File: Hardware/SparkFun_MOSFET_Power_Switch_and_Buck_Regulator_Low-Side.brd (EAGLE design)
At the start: 38.1 x 38.1 mm, 79 parts, among them J1 PTH, J3 5.5x2.1mm Barrel, J4 SMD, Q1 600mA/40V, Q2 100A/100V/6.8mΩ, U1 LMR14203

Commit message: Update silk to match product name
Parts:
- removed U$34: (no value), output:SIDE2
- removed U$35: (no value), output:LOW3
- added U$39: (no value), output:BUCK5
- added U$40: (no value), output:REGULATOR6
- added U$41: (no value), output:#_BUCK_REG7
- added U$42: (no value), output:AND8
- added U$43: (no value), output:LOW0
- added U$44: (no value), output:SIDE0
- moved U$8 29.9 mm to (30.6, 33.7)
- moved U$33 1.01 mm to (35.2, 6.68)
- moved U$23 1.01 mm to (31.4, 6.68)
- moved U$13 0.49 mm to (33.2, 9.38)
- moved U$9 0.49 mm to (33.4, 10.6)
- moved U$2 0.49 mm to (33.4, 11.8)
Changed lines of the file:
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@@
 <layer number="45" name="Holes" color="7" fill="1" visible="yes" active="yes"/>
 <layer number="46" name="Milling" color="3" fill="1" visible="no" active="yes"/>
-<layer number="47" name="Measures" color="7" fill="1" visible="yes" active="yes"/>
+<layer number="47" name="Measures" color="7" fill="1" visible="no" active="yes"/>
 <layer number="48" name="Document" color="7" fill="1" visible="no" active="yes"/>
 <layer number="49" name="Reference" color="7" fill="1" visible="yes" active="yes"/>
@@
 <dimension x1="2.54" y1="0" x2="1.27" y2="8.89" x3="-8.89" y3="4.445" textsize="1.27" layer="47" dtype="vertical" unit="inch"/>
 <text x="8.89" y="53.34" size="1.27" layer="47" font="vector">Units are INCHES</text>
-<wire x1="33.169859375" y1="7.622540625" x2="33.72611875" y2="7.622540625" width="0.2032" layer="21"/>
-<wire x1="19.535140625" y1="11.752575" x2="18.75028125" y2="11.752575" width="0.3048" layer="22"/>
+<wire x1="32.992059375" y1="6.63194375" x2="33.54831875" y2="6.63194375" width="0.2032" layer="21"/>
 <wire x1="25.072340625" y1="22.76348125" x2="25.072340625" y2="20.403821875" width="0.2032" layer="21"/>
 <wire x1="18.313396875" y1="27.523440625" x2="20.67305625" y2="27.523440625" width="0.2032" layer="21"/>
@@
 <dimension x1="0" y1="0" x2="13.78711875" y2="3.5179" x3="6.893559375" y3="-2.745740625" textsize="1.27" layer="47" dtype="horizontal" unit="inch"/>
 <dimension x1="2.54" y1="0" x2="13.78711875" y2="3.520440625" x3="-5.715" y3="1.76021875" textsize="1.27" layer="47" dtype="vertical" unit="inch"/>
+<wire x1="29.842528125" y1="6.175046875" x2="29.84576875" y2="7.1739875" width="0.1524" layer="21" curve="-123.9914"/>
+<wire x1="36.712675" y1="7.13223125" x2="36.709434375" y2="6.133290625" width="0.1524" layer="21" curve="-123.9914"/>
+<wire x1="19.822159375" y1="9.347203125" x2="19.2659" y2="9.347203125" width="0.2032" layer="22"/>
+<wire x1="22.971690625" y1="8.89030625" x2="22.96845" y2="9.889246875" width="0.1524" layer="22" curve="123.9914"/>
+<wire x1="16.10154375" y1="9.847490625" x2="16.104784375" y2="8.84855" width="0.1524" layer="22" curve="123.9914"/>
 </plain>
 <attributes>
@@
 <element name="U$20" library="output" package="#0" value="" x="1.27" y="13.462" smashed="yes" rot="MR270"/>
 <element name="U$22" library="output" package="#1" value="" x="1.27" y="6.35" smashed="yes" rot="MR270"/>
-<element name="U$2" library="output" package="MOSFET0" value="" x="33.54578125" y="11.3512625" smashed="yes"/>
-<element name="U$9" library="output" package="POWER1" value="" x="33.54831875" y="10.119359375" smashed="yes"/>
-<element name="U$13" library="output" package="SWITCH2" value="" x="33.347659375" y="8.930640625" smashed="yes"/>
+<element name="U$2" library="output" package="MOSFET0" value="" x="33.352740625" y="11.803384375" smashed="yes"/>
+<element name="U$9" library="output" package="POWER1" value="" x="33.355278125" y="10.57148125" smashed="yes"/>
+<element name="U$13" library="output" package="SWITCH2" value="" x="33.15461875" y="9.3827625" smashed="yes"/>
 <element name="MEAS" library="SparkFun-Jumpers" package="COMBO-JUMPER_2_NC_TRACE" value="JUMPER-COMBO_2_NC_TRACE" x="5.715" y="16.51" smashed="yes" rot="MR180">
 <attribute name="NAME" x="5.715" y="15.367" size="0.6096" layer="26" font="vector" ratio="20" rot="MR180" align="bottom-center"/>
@@
 <element name="U$7" library="output" package="#ON#10" value="" x="13.843" y="2.2098" smashed="yes"/>
 <element name="LOGO2" library="SparkFun-Aesthetics" package="SFE_LOGO_NAME_FLAME_.2" value="SFE_LOGO_NAME_FLAME.2_INCH" x="18.823940625" y="21.887178125" smashed="yes" rot="MR0"/>
-<element name="U$8" library="SparkFun-Aesthetics" package="SFE_LOGO_FLAME_.2" value="" x="31.2191375" y="3.810003125" smashed="yes"/>
+<element name="U$8" library="SparkFun-Aesthetics" package="SFE_LOGO_FLAME_.2" value="" x="30.5841375" y="33.655003125" smashed="yes"/>
 <element name="PWR_LED" library="SparkFun-Jumpers" package="SMT-JUMPER_2_NC_TRACE_SILK" package3d_urn="urn:adsk.eagle:package:39281/1" value="" x="36.195" y="30.48" smashed="yes" rot="MR90">
 <attribute name="NAME" x="37.338" y="30.48" size="0.6096" layer="26" font="vector" ratio="20" rot="MR90" align="bottom-center"/>
@@
 <element name="FD4" library="SparkFun-Aesthetics" package="FIDUCIAL-MICRO" value="FIDUCIALUFIDUCIAL" x="33.02" y="36.83" smashed="yes"/>
 <element name="U$17" library="output" package="#MEAS#14" value="" x="5.737859375" y="18.209259375" smashed="yes" rot="MR0"/>
-<element name="U$23" library="output" package="LOW0" value="" x="31.607759375" y="7.665721875" smashed="yes"/>
-<element name="U$33" library="output" package="SIDE0" value="" x="35.417759375" y="7.665721875" smashed="yes"/>
-<element name="U$34" library="output" package="SIDE2" value="" x="15.651478125" y="11.79575625" smashed="yes" rot="MR0"/>
-<element name="U$35" library="output" package="LOW3" value="" x="22.136103125" y="11.927834375" smashed="yes" rot="MR0"/>
+<element name="U$23" library="output" package="LOW0" value="" x="31.429959375" y="6.675125" smashed="yes"/>
+<element name="U$33" library="output" package="SIDE0" value="" x="35.239959375" y="6.675125" smashed="yes"/>
 <element name="J6" library="SparkFun-Connectors" package="1X02_NO_SILK" value="" x="8.89" y="36.83" smashed="yes">
 <attribute name="NAME" x="7.62" y="38.227" size="0.6096" layer="25" font="vector" ratio="20"/>
@@
 <element name="U$38" library="output" package="#MEAS#14" value="" x="10.284459375" y="16.532859375" smashed="yes"/>
 <element name="LOGO3" library="SparkFun-Aesthetics" package="ORDERING_INSTRUCTIONS" value="SPECIAL_INSTRUCTIONS-ORDERING" x="64.77" y="50.8" smashed="yes"/>
+<element name="U$39" library="output" package="BUCK5" value="" x="22.96921875" y="10.970259375" smashed="yes" rot="MR0"/>
+<element name="U$40" library="output" package="REGULATOR6" value="" x="17.25421875" y="10.970259375" smashed="yes" rot="MR0"/>
+<element name="U$41" library="output" package="#_BUCK_REG7" value="" x="33.461959375" y="8.072121875" smashed="yes"/>
+<element name="U$42" library="output" package="AND8" value="" x="19.072859375" y="12.430759375" smashed="yes" rot="MR0"/>
+<element name="U$43" library="output" package="LOW0" value="" x="21.384259375" y="9.390384375" smashed="yes" rot="MR0"/>
+<element name="U$44" library="output" package="SIDE0" value="" x="17.574259375" y="9.390384375" smashed="yes" rot="MR0"/>
 </elements>
 <signals>
@@
 <via x="5.466078125" y="10.195559375" extent="1-16" drill="0.3048"/>
 <via x="15.9385" y="4.831078125" extent="1-16" drill="0.3048"/>
-<via x="31.793178125" y="1.3843" extent="1-16" drill="0.3048"/>
-<via x="37.152578125" y="6.215378125" extent="1-16" drill="0.3048"/>
+<via x="32.46881875" y="0.7874" extent="1-16" drill="0.3048"/>
+<via x="37.371015625" y="5.435596875" extent="1-16" drill="0.3048"/>
 <via x="37.203378125" y="32.369759375" extent="1-16" drill="0.3048"/>
 <via x="31.666178125" y="36.91381875" extent="1-16" drill="0.3048"/>

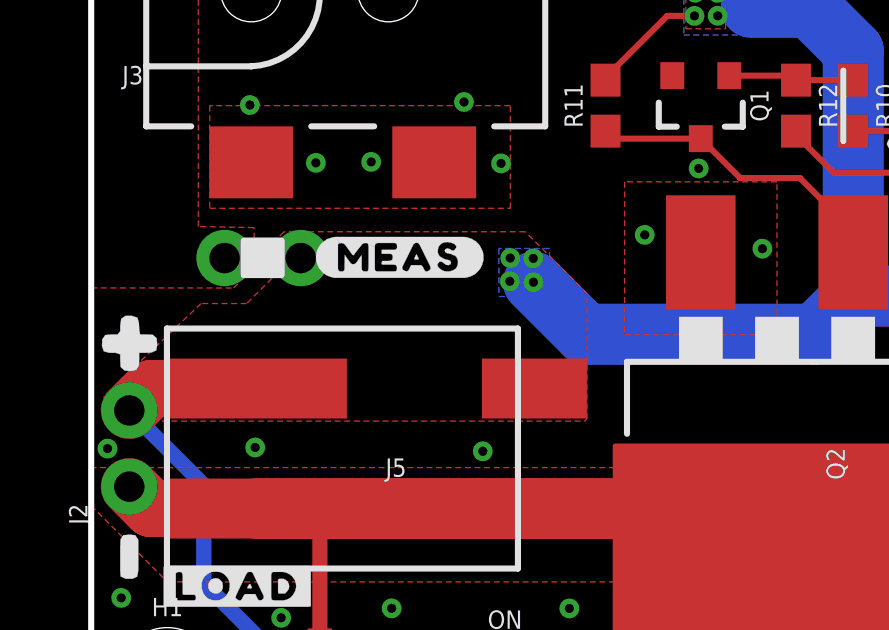
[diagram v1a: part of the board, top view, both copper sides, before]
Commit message: Added D1 Zener
-Added D1 to clamp spike on VCC and protect U1 and C4
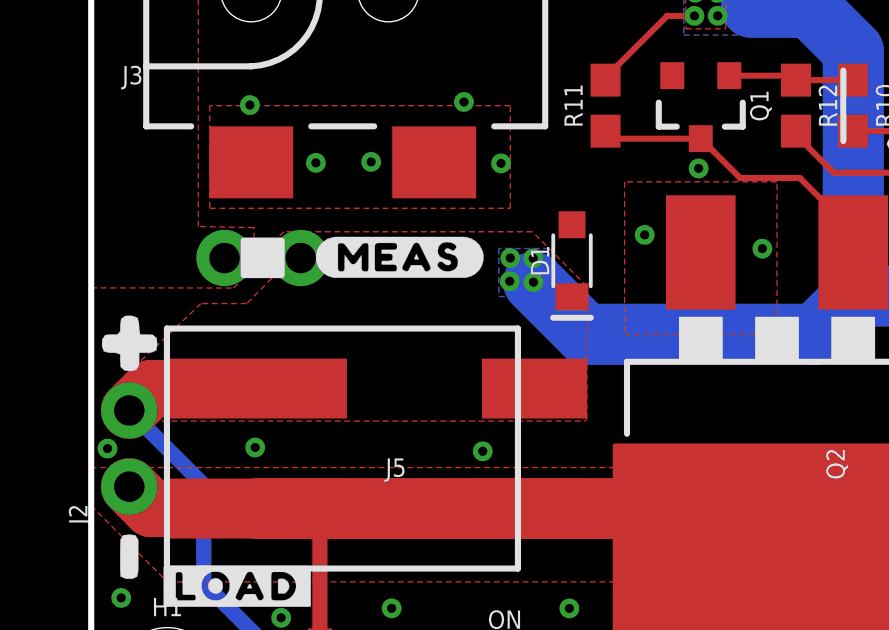
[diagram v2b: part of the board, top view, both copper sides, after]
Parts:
- added D1: 15V, SparkFun-DiscreteSemi:PANASONIC_SMINI2-F5-B
- J4: value SMD -> 1X04_SMD_STRAIGHT_COMBO
- ON, POWER: value RED -> Red
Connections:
- net GND: now also D1.A
- net VCC: now also D1.C
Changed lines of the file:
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@@
 <layer number="27" name="tValues" color="7" fill="1" visible="no" active="yes"/>
 <layer number="28" name="bValues" color="7" fill="1" visible="no" active="yes"/>
-<layer number="29" name="tStop" color="7" fill="6" visible="no" active="yes"/>
+<layer number="29" name="tStop" color="7" fill="6" visible="yes" active="yes"/>
 <layer number="30" name="bStop" color="7" fill="3" visible="no" active="yes"/>
 <layer number="31" name="tCream" color="7" fill="5" visible="no" active="yes"/>
@@
 <attribute name="VALUE" x="2.54" y="33.528" size="0.6096" layer="27" font="vector" ratio="20" align="top-center"/>
 </element>
-<element name="ON" library="SparkFun-LED" package="LED-0603" value="RED" x="13.7922" y="3.5179" smashed="yes">
+<element name="ON" library="SparkFun-LED" package="LED-0603" value="Red" x="13.7922" y="3.5179" smashed="yes">
 <attribute name="NAME" x="13.7922" y="4.1529" size="0.6096" layer="25" font="vector" ratio="20" align="bottom-center"/>
 <attribute name="PROD_ID" value="DIO-17976" x="13.7922" y="7.3279" size="1.778" layer="27" font="vector" ratio="15" display="off"/>
+<attribute name="VALUE" value="Red" x="13.7922" y="3.5179" size="1.778" layer="27" display="off"/>
 </element>
 <element name="R2" library="SparkFun-Resistors" package="0603" value="4.7k" x="10.1498375" y="2.519678125" smashed="yes" rot="R270">
@@
 <attribute name="VALUE" x="5.715" y="17.653" size="0.6096" layer="28" font="vector" ratio="20" rot="MR180" align="top-center"/>
 </element>
-<element name="POWER" library="SparkFun-LED" package="LED-0603" value="RED" x="33.655" y="29.21" smashed="yes">
+<element name="POWER" library="SparkFun-LED" package="LED-0603" value="Red" x="33.655" y="29.21" smashed="yes">
 <attribute name="NAME" x="33.655" y="29.845" size="0.6096" layer="25" font="vector" ratio="20" align="bottom-center"/>
 <attribute name="PROD_ID" value="DIO-17976" x="33.655" y="29.21" size="1.778" layer="27" font="vector" ratio="15" display="off"/>
+<attribute name="VALUE" value="Red" x="33.655" y="29.21" size="1.778" layer="27" display="off"/>
 </element>
 <element name="R1" library="SparkFun-Resistors" package="0603" value="4.7k" x="33.6423" y="30.8737" smashed="yes" rot="R180">
@@
 <element name="U$25" library="output" package="POWER_1" value="" x="18.696940625" y="16.5735" smashed="yes" rot="MR0"/>
 <element name="U$26" library="output" package="SWITCH_2" value="" x="18.760440625" y="14.23161875" smashed="yes" rot="MR0"/>
-<element name="J4" library="SparkFun-Connectors" package="1X04_SMD_VERTICAL_COMBO" value="SMD" x="33.02" y="22.86" smashed="yes" rot="R270">
+<element name="J4" library="SparkFun-Connectors" package="1X04_SMD_VERTICAL_COMBO" value="1X04_SMD_STRAIGHT_COMBO" x="33.02" y="22.86" smashed="yes" rot="R270">
 <attribute name="NAME" x="35.878" y="23.241" size="0.6096" layer="25" font="vector" ratio="20" rot="R270"/>
 <attribute name="PROD_ID" value="CONN-08511" x="33.02" y="22.86" size="1.778" layer="27" rot="R270" display="off"/>
@@
 <element name="U$43" library="output" package="LOW0" value="" x="21.384259375" y="9.390384375" smashed="yes" rot="MR0"/>
 <element name="U$44" library="output" package="SIDE0" value="" x="17.574259375" y="9.390384375" smashed="yes" rot="MR0"/>
+<element name="D1" library="SparkFun-DiscreteSemi" package="PANASONIC_SMINI2-F5-B" value="15V" x="16.0274" y="16.418559375" smashed="yes" rot="R90">
+<attribute name="NAME" x="15.2654" y="16.418559375" size="0.6096" layer="25" font="vector" ratio="20" rot="R90" align="bottom-center"/>
+<attribute name="PROD_ID" value="DIO-12989" x="16.0274" y="16.418559375" size="1.778" layer="27" rot="R90" display="off"/>
+<attribute name="VALUE" x="16.7894" y="16.418559375" size="0.6096" layer="27" font="vector" ratio="20" rot="R90" align="top-center"/>
+</element>
 </elements>
 <signals>
@@
 </polygon>
 <via x="0.543559375" y="10.15745625" extent="1-16" drill="0.3048"/>
+<contactref element="D1" pad="A"/>
 </signal>
 <signal name="SDA1">
@@
 <wire x1="3.75158125" y1="8.94841875" x2="3.75158125" y2="5.6794375" width="0.508" layer="16"/>
 <polygon width="0.2032" layer="1" thermals="no">
-<vertex x="14.46784375" y="17.3863"/>
+<vertex x="14.7066" y="17.3863"/>
 <vertex x="6.426196875" y="17.3863"/>
 <vertex x="6.0198" y="16.979903125"/>
@@
 <vertex x="16.4465" y="11.0744"/>
 <vertex x="16.527778125" y="11.154525"/>
-<vertex x="16.527778125" y="15.326365625"/>
+<vertex x="16.527778125" y="15.565121875"/>
 </polygon>
 <via x="13.97" y="16.51" extent="1-16" drill="0.3048"/>
@@
 <wire x1="16.47698125" y1="13.97" x2="24.13" y2="13.97" width="2.032" layer="16"/>
 <wire x1="24.13" y1="13.97" x2="25.4" y2="15.24" width="2.032" layer="16"/>
+<contactref element="D1" pad="C"/>
 </signal>
 <signal name="N$1">
